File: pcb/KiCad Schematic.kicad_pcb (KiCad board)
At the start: 2 copper layers, 50.1 x 70 mm, 90 parts, among them IC1 MC7805BDTRKG, IC2 ATSAMD51J19A-MU, J1 47309-3351, J10 Conn_01x04, J11 Conn_01x04, J12 Conn_01x03, J13 Conn_01x03, J14 Conn_01x20, J15 Conn_01x03, J16 Conn_01x03, J17 Hole, J18 Hole, J19 Hole, J2 Conn_01x02, J20 Hole, J21 Conn_01x02, J3 47346-0001, J4 Conn_01x04, J5 Conn_01x04, J6 20021121-00010C4LF, J7 Conn_01x02, J8 Conn_01x02, J9 Conn_01x02, Q1 NVTFS5C680NLTAG, Q2 NVTFS5C680NLTAG, U1 TMC2041-LA, U2 TMC2041-LA, U3 AP2112K-3.3, Y1 LFXTAL009678REEL

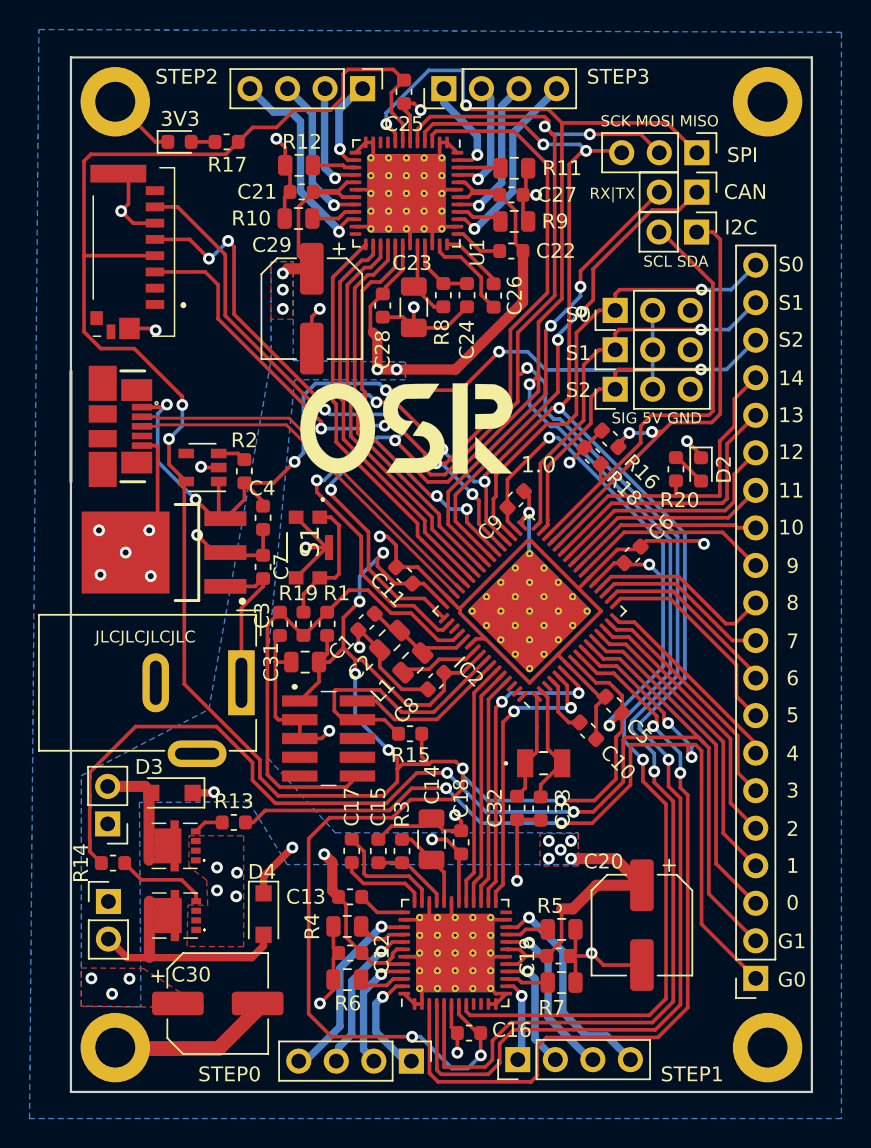
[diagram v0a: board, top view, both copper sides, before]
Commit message: rename folder for clarity. Versioning handled by git tags
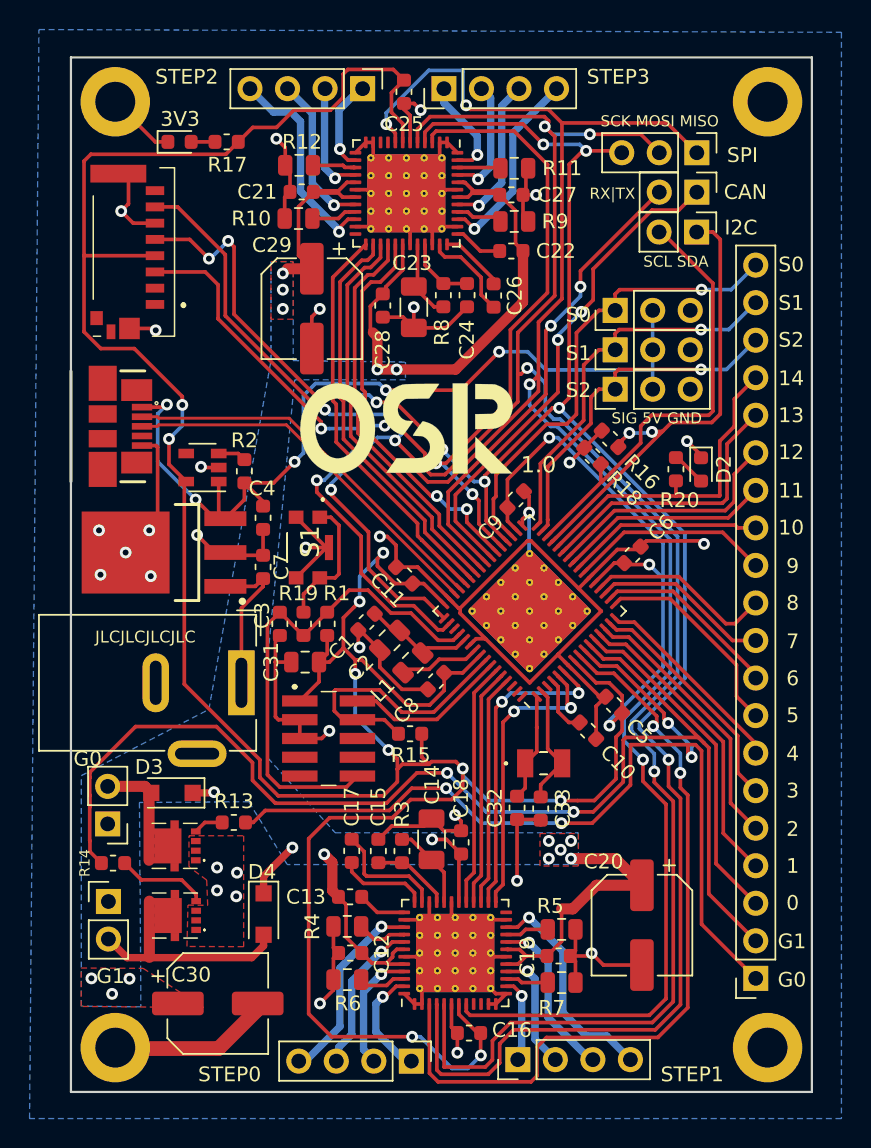
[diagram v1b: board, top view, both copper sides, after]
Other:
- board text added: ""I really like ceilings... I guess you could call me a ceiling fan" -Unknown"
- board text removed: ""2 potatoes don't make a potato" -George Washington"
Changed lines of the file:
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@@
   (general
     (thickness 1.6)
-    (drawings 42)
+    (drawings 44)
     (tracks 1380)
     (zones 0)
@@
     (tags "QFN DFN_QFN")
     (attr smd)
-    (fp_text reference IC2 (at 0 -5.82 135) (layer F.SilkS)
+    (fp_text reference IC2 (at 0 -5.819999 135) (layer F.SilkS) hide
       (effects (font (size 1 1) (thickness 0.15)))
     )
@@
     (tags resistor)
     (attr smd)
-    (fp_text reference R14 (at 2.1625 0 90) (layer F.SilkS)
-      (effects (font (size 1 1) (thickness 0.15)))
+    (fp_text reference R14 (at 1.9125 0 90) (layer F.SilkS)
+      (effects (font (size 0.7 0.7) (thickness 0.1)))
     )
     (fp_text value 174 (at 0 1.43) (layer F.Fab)
@@
     (tags "QFN DFN_QFN")
     (attr smd)
-    (fp_text reference U1 (at 4 -4.8 90) (layer F.SilkS)
+    (fp_text reference U1 (at 4 -4.8 90) (layer F.SilkS) hide
       (effects (font (size 1 1) (thickness 0.15)))
     )
@@
     )
   )
-  (gr_text "\"2 potatoes don't\nmake a potato\"\n-George Washington" (at 19.7 136.3) (layer B.SilkS)
+  (gr_text G1 (at 21.55 188.05) (layer F.SilkS)
+    (effects (font (size 1 1) (thickness 0.2)))
+  )
+  (gr_text G0 (at 20 173.35) (layer F.SilkS)
+    (effects (font (size 1 1) (thickness 0.2)))
+  )
+  (gr_text "\"I really like ceilings...\nI guess you could call\nme a ceiling fan\"\n-Unknown" (at 19.7 136.3) (layer B.SilkS)
     (effects (font (size 1.5 1.5) (thickness 0.25)) (justify right mirror))
   )

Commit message: add power header
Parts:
- added J22: Conn_01x06, Connector_PinSocket_2.54mm:PinSocket_1x06_P2.54mm_Vertical, F.Cu at (29.8, 135.3)
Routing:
- net +5V: track 59.7 -> 72.9 mm, vias 5 -> 7
- net +3V3: track 253.1 -> 261.3 mm
- net +VDC: track 101.3 -> 109.1 mm, vias 17 -> 10
- net /MISO: track 169.6 -> 172.0 mm
- net /MOSI: track 168.0 -> 168.8 mm
- net /D1_CS: track 40.7 -> 40.0 mm
- net GND: track 218.5 -> 217.9 mm, vias 30 -> 35
- net /SCK: track 148.3 -> 148.0 mm, vias 10 -> 8
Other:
- board text added: "1.1"
- board text added: "5V"
- board text added: "GND"
- board text added: "VDC"
- board text removed: "1.0"

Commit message: resolve a few issues in pcb design
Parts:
- added C34: 10uF, Capacitor_SMD:C_0805_2012Metric, F.Cu at (28.2, 157.4)
- added C35: 10uF, Capacitor_SMD:C_0805_2012Metric, F.Cu at (30.3, 160.9)
- added C36: 10uF, Capacitor_SMD:C_0805_2012Metric, F.Cu at (30.3, 157.4)
- added L2: 10uH, Inductor_SMD:L_0805_2012Metric, F.Cu at (26.2, 160.9)
- added L3: 10uH, Inductor_SMD:L_0805_2012Metric, F.Cu at (28.2, 160.9)
- C4: value 1uF -> 100nF
- IC1: value MC7805BDTRKG -> AP63205WU-7; footprint SamacSys_Parts:TO229P990X238-4N -> SamacSys_Parts:SOT95P280X100-6N
- moved C7 9.94 mm to (22.2, 157.9), turned to 0 degrees
- moved C4 5.94 mm to (25.9, 157.5), turned to 90 degrees
- moved IC1 2.68 mm to (22.8, 160.7), turned to 0 degrees
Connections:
- C4 pad 1: +5V -> Net-(C4-Pad1)
- C4 pad 2: GND -> Net-(C4-Pad2)
- IC1 pad 1: +VDC -> +5V
- IC1 pad 2: GND -> +VDC
- IC1 pad 3: +5V -> +VDC
- IC2 pad 51: Net-(IC2-Pad51) -> /SD_CS
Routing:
- net /SD_CS: track 0.00 -> 43.1 mm, vias 0 -> 4
- net +5V: track 72.9 -> 88.9 mm
- net +3V3: track 261.3 -> 274.6 mm
- net +VDC: track 109.1 -> 115.3 mm
- net Net-(C4-Pad1): track 0.00 -> 6.18 mm
- net GND: track 217.9 -> 213.8 mm, vias 35 -> 32
- net Net-(C4-Pad2): track 0.00 -> 3.72 mm
- net /MISO: track 172.0 -> 172.1 mm, vias 7 -> 9

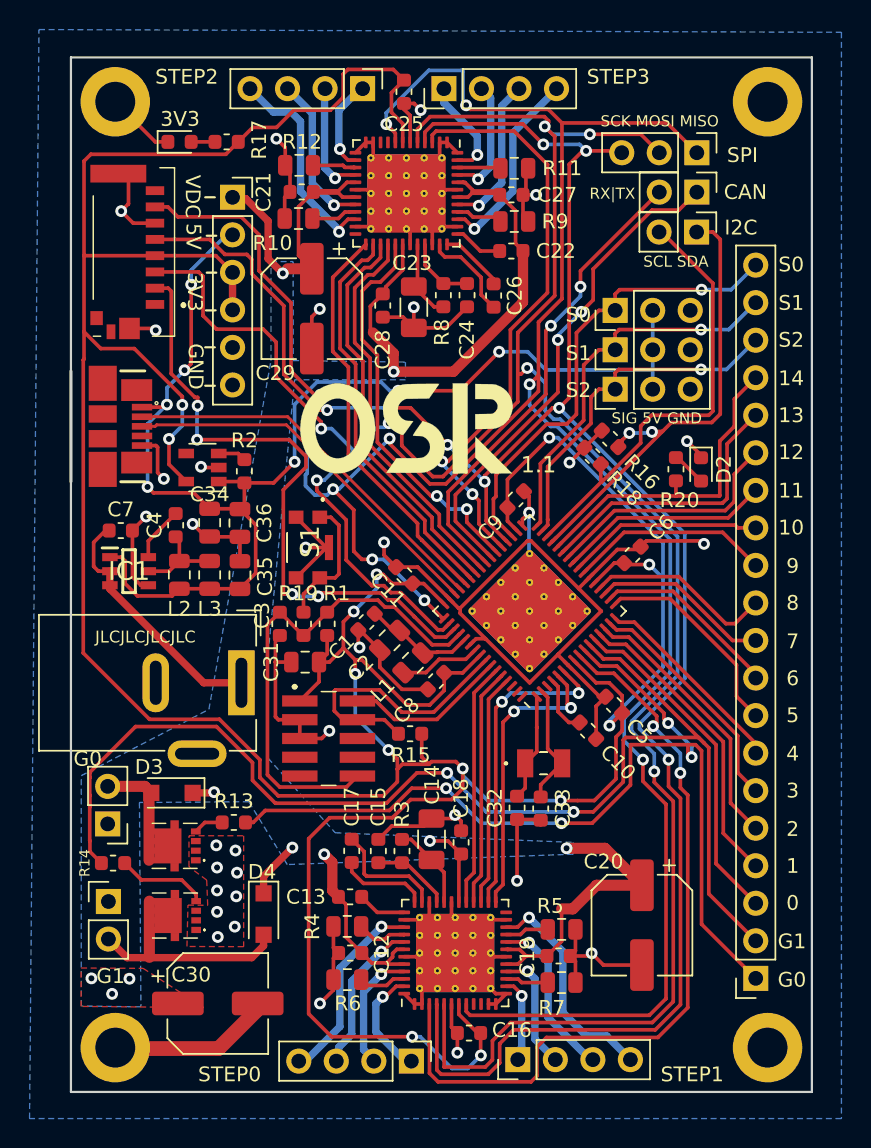
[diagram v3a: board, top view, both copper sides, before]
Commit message: pcb optimizations and fixes to v1 arduino package
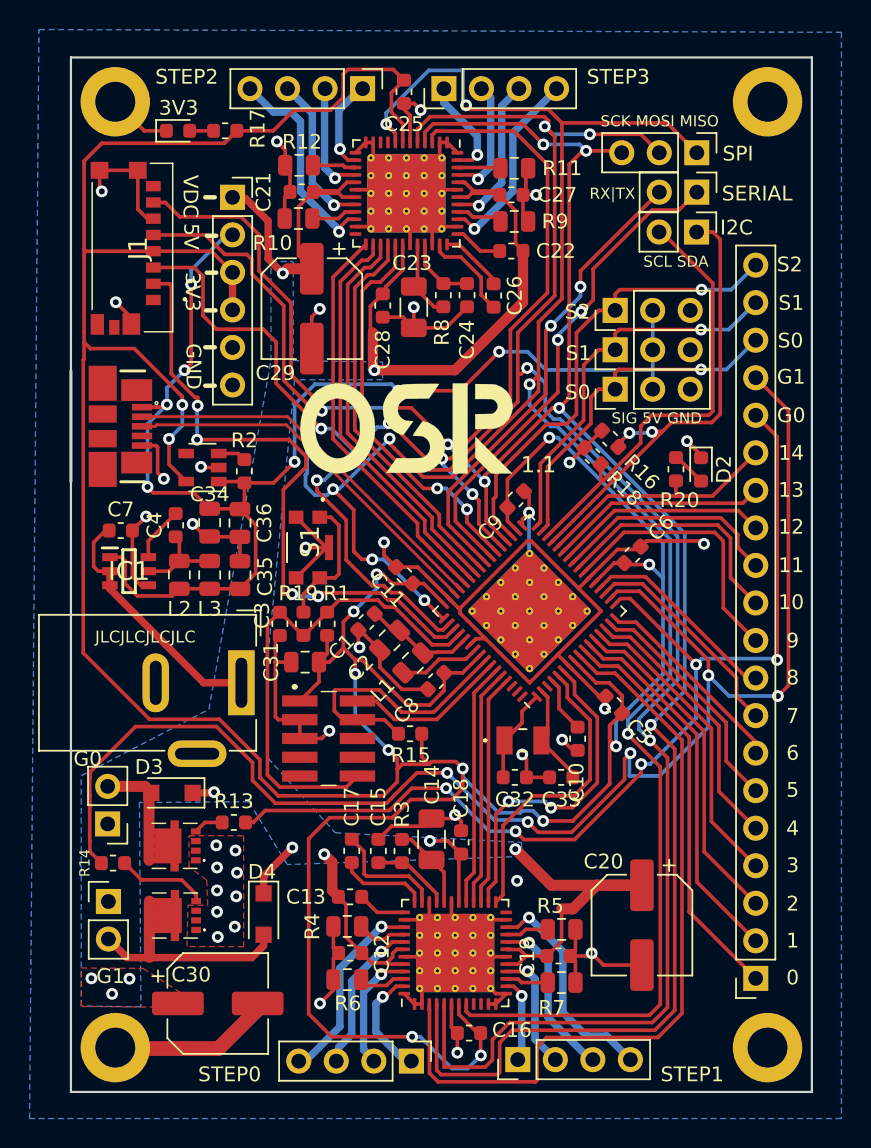
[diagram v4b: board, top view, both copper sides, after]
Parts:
- J1: value 47309-3351 -> 47571-0001; footprint SamacSys_Parts:473093351 -> SamacSys_Parts:475710001
- moved C33 2.53 mm to (52.0, 174.6), turned to 180 degrees
- moved Y1 2.09 mm to (49.5, 172.1)
- moved C32 2.07 mm to (48.9, 174.6), turned to 180 degrees
- moved C10 0.88 mm to (53.1, 172.0), turned to 270 degrees
- moved D1 0.76 mm to (26.1, 130.8)
- moved R17 0.76 mm to (29.3, 130.8)
- moved J1 0.48 mm to (23.0, 138.8)
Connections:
- IC2 pad 10: /GATE0 -> /GEN0
- IC2 pad 11: /GATE1 -> /GEN1
- IC2 pad 12: /GEN0 -> /GEN2
- IC2 pad 13: /GEN1 -> /GEN3
- IC2 pad 14: /GEN2 -> /GEN4
- IC2 pad 15: /GEN3 -> /GEN5
- IC2 pad 16: /GEN4 -> /GEN6
- IC2 pad 17: /GEN5 -> /GATE0
- IC2 pad 18: /GEN6 -> /GATE1
- IC2 pad 31: /SERVO2 -> /SERVO0
- IC2 pad 35: /SERVO0 -> /SERVO2
- J1 pad G3: Net-(J1-PadG3) -> GND
- J13 pad 1: /SERVO0 -> /SERVO2
- J14 pad 1: /GATE0 -> /GEN0
- J14 pad 10: /GEN7 -> /GEN9
- J14 pad 11: /GEN8 -> /GEN10
- J14 pad 12: /GEN9 -> /GEN11
- J14 pad 13: /GEN10 -> /GEN12
- J14 pad 14: /GEN11 -> /GEN13
- J14 pad 15: /GEN12 -> /GEN14
- J14 pad 16: /GEN13 -> /GATE0
- J14 pad 17: /GEN14 -> /GATE1
- J14 pad 18: /SERVO2 -> /SERVO0
- J14 pad 2: /GATE1 -> /GEN1
- J14 pad 20: /SERVO0 -> /SERVO2
- J14 pad 3: /GEN0 -> /GEN2
- J14 pad 4: /GEN1 -> /GEN3
- J14 pad 5: /GEN2 -> /GEN4
- J14 pad 6: /GEN3 -> /GEN5
- J14 pad 7: /GEN4 -> /GEN6
- J14 pad 8: /GEN5 -> /GEN7
- J14 pad 9: /GEN6 -> /GEN8
- J16 pad 1: /SERVO2 -> /SERVO0
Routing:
- net /GATE1: track 83.7 -> 102.4 mm, vias 2 -> 5
- net /SERVO2: track 23.8 -> 32.1 mm
- net /SERVO0: track 32.1 -> 23.8 mm
- net /GATE0: track 65.6 -> 70.6 mm, vias 4 -> 5
- net /GEN14: track 22.4 -> 17.4 mm
- net /GEN9: track 13.7 -> 18.5 mm
- net /GEN3: track 16.0 -> 20.8 mm
- net /GEN2: track 18.4 -> 23.1 mm
- net /GEN1: track 20.7 -> 25.4 mm
- net /GEN0: track 23.0 -> 27.8 mm
- net /GEN13: track 19.1 -> 14.9 mm
- net /GEN4: track 14.3 -> 18.4 mm
- net +VDC: track 115.3 -> 119.4 mm
- net /GEN10: track 13.3 -> 17.0 mm
- net /GEN7: track 12.1 -> 14.9 mm
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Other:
- board text added: ""I'm not superstitious, but I am a little stitious" -M. Scott"
- board text added: "SERIAL"
- board text removed: ""I really like ceilings... I guess you could call me a ceiling fan" -Unknown"
- board text removed: "CAN"

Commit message: pcb v2 release
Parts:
- added R21: 100k, Resistor_SMD:R_0603_1608Metric, F.Cu at (42.4, 172.7)
- added R22: 10k, Resistor_SMD:R_0603_1608Metric, F.Cu at (44.0, 172.7)
- moved R15 1.42 mm to (40.9, 172.7), turned to 90 degrees
- moved C32 0.36 mm to (49.1, 174.9)
- moved C33 0.36 mm to (52.2, 174.9)
- moved Y1 0.36 mm to (49.6, 172.4)
- moved C10 0.36 mm to (53.4, 172.3)
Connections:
- IC2 pad 62: Net-(IC2-Pad62) -> /VSENSE
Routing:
- net /VSENSE: track 0.00 -> 8.51 mm, vias 0 -> 2
- net +VDC: track 119.4 -> 125.8 mm, vias 10 -> 11
- net +3V3: track 277.3 -> 273.4 mm, vias 14 -> 15
- net /OSC0: track 8.06 -> 6.62 mm
- net /GATE1: track 102.4 -> 103.3 mm
- net /D0_S1_STEP: track 22.8 -> 23.6 mm
- net /OSC1: track 7.88 -> 8.69 mm
- net /D0_S1_DIR: track 20.5 -> 21.2 mm
- net /GATE0: track 70.6 -> 71.1 mm
- net GND: track 212.3 -> 211.8 mm, vias 35 -> 36
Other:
- board text added: "2.0"
- board text removed: "1.1"

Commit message: arduino version bump
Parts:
- added D5: CGRTS4004-HF, Diode_SMD:D_SOD-123F, F.Cu at (22.9, 161.8)
- moved C7 2.27 mm to (23.6, 156.1)
- moved C36 2.10 mm to (28.2, 157.4)
- moved C34 2.05 mm to (30.3, 157.4)
- moved IC1 1.91 mm to (23.0, 158.8)
- moved R2 0.30 mm to (30.6, 153.6)
- moved U3 0.30 mm to (27.8, 153.3)
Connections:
- C36 pad 1: +5V -> +3V3
- C7 pad 1: +VDC -> Net-(C7-Pad1)
- IC1 pad 2: +VDC -> Net-(C7-Pad1)
- IC1 pad 3: +VDC -> Net-(C7-Pad1)
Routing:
- net Net-(C7-Pad1): track 0.00 -> 7.96 mm
- net +VDC: track 125.8 -> 119.2 mm
- net +5V: track 88.8 -> 85.4 mm
- net +3V3: track 273.4 -> 276.3 mm
- net Net-(C4-Pad2): track 3.72 -> 2.08 mm
- net GND: track 211.8 -> 213.2 mm, vias 36 -> 35
- net Net-(C4-Pad1): track 6.18 -> 5.62 mm
